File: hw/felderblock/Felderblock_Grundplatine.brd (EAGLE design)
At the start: 100 x 78 mm, 52 parts, among them IC2 LM2936, IC3 ULN2803, IC4 MCP2300X/P, J1 RJ11, J2 RJ11, M1 ARDUINO-NANO-3.0, T2 BC337, X1 TASTENSPERRE1, X2 TASTENSPERRE2, X3 SCHLUESSELSPERRE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

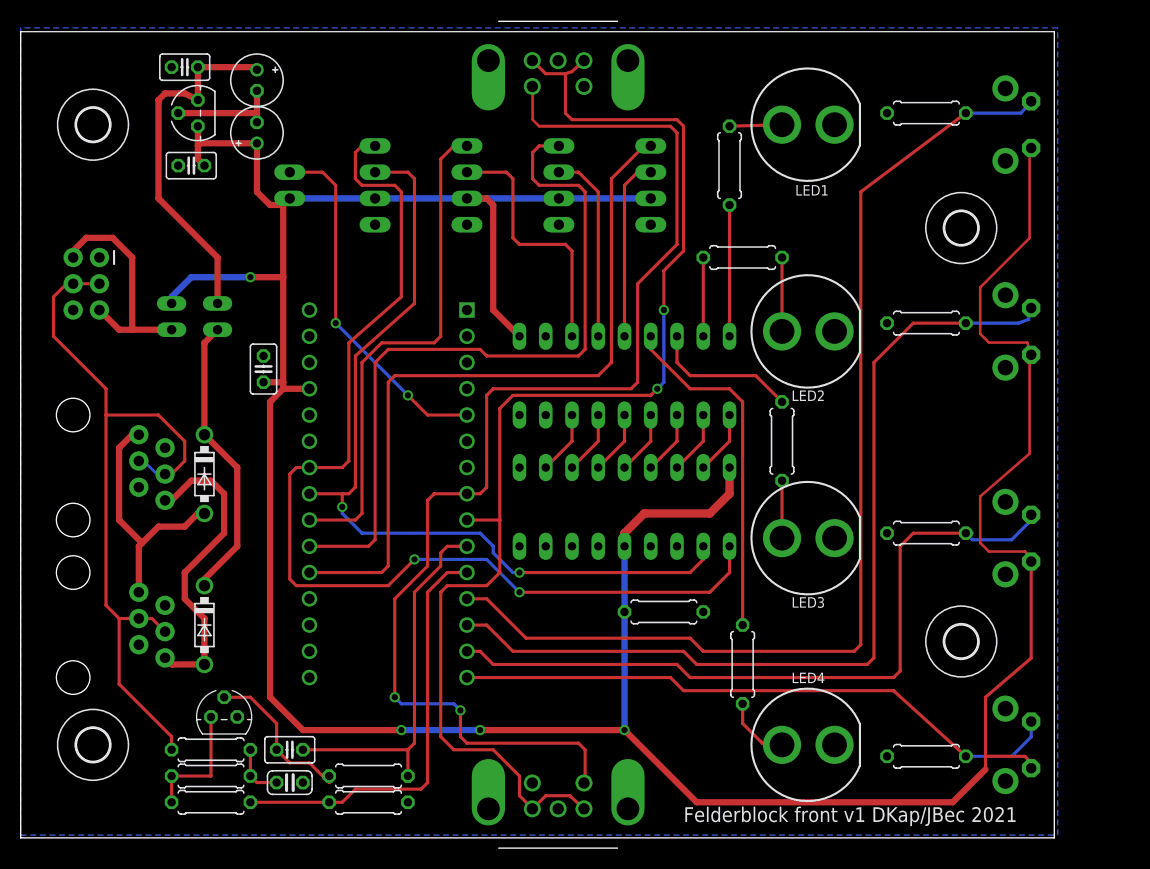
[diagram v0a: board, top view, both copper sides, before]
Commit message: CW and CCW split
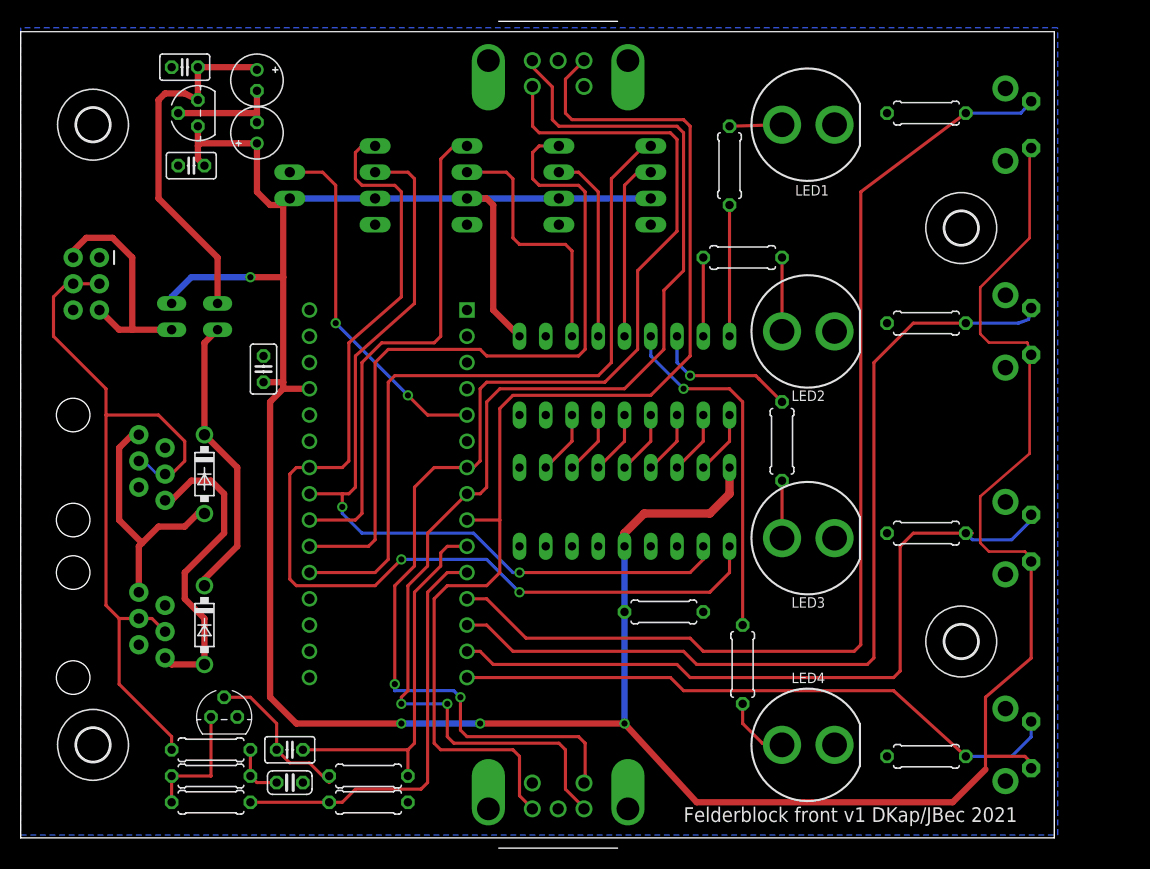
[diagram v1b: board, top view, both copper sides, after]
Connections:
- new net MI_REV: M1.J1.8, S5.A, S6.A
- net MI_FWD: no longer S5.A, S6.A
- net MI_SW: now also M1.J1.7; no longer M1.J1.8
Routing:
- net MI_REV: track 0.00 -> 120.1 mm, vias 0 -> 2
- net MI_FWD: track 123.0 -> 116.0 mm, vias 2 -> 0
- net MI_SW: track 121.4 -> 118.2 mm
- net FELD4_LEDD: track 33.9 -> 34.2 mm, vias 0 -> 1
- net FELD3_LEDD: vias 0 -> 1

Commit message: changed I2C connectors
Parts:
- removed X4: I2C, con-molex:22-23-2041
- added I2C: (no value), SparkFun-Connectors:JST-4-PTH-VERT
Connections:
- net +5V: now also I2C.3; no longer X4.2
- net GND: now also I2C.4; no longer X4.1
- net SCL: now also I2C.1; no longer X4.4
- net SDA: now also I2C.2; no longer X4.3
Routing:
- net SCL: track 102.9 -> 96.9 mm
- net SDA: track 82.2 -> 77.6 mm
- net +5V: vias 4 -> 5
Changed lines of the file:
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@@
 <?xml version="1.0" encoding="utf-8"?>
 <!DOCTYPE eagle SYSTEM "eagle.dtd">
-<eagle version="7.6.0">
+<eagle version="7.7.0">
 <drawing>
 <settings>
@@
 <attribute name="VALUE" x="67.945" y="45.085" size="1.27" layer="28" ratio="10" rot="MR0"/>
 </element>
-<element name="X4" library="con-molex" package="22-23-2041" value="I2C" x="34.29" y="64.135" smashed="yes" rot="MR90">
-<attribute name="MF" value="MOLEX" x="34.29" y="64.135" size="1.778" layer="28" rot="MR90" display="off"/>
-<attribute name="OC_NEWARK" value="38C0355" x="34.29" y="64.135" size="1.778" layer="28" rot="MR90" display="off"/>
-<attribute name="MPN" value="22-23-2041" x="34.29" y="64.135" size="1.778" layer="28" rot="MR90" display="off"/>
-<attribute name="OC_FARNELL" value="1462920" x="34.29" y="64.135" size="1.778" layer="28" rot="MR90" display="off"/>
-<attribute name="VALUE" x="38.1" y="59.055" size="1.016" layer="28" ratio="10" rot="MR90"/>
-</element>
 <element name="S5" library="alps" package="EC11B42" value="EC11B42AE" x="52" y="76.2" smashed="yes" rot="MR180">
 <attribute name="NAME" x="48.19" y="72.39" size="1.27" layer="26" rot="MR180"/>
@@
 <element name="C7" library="resistor" package="C025-025X050" value="1nF" x="26.035" y="9.525" smashed="yes" rot="R180">
 <attribute name="VALUE" x="28.321" y="12.319" size="1.27" layer="27" ratio="10" rot="R180"/>
+</element>
+<element name="I2C" library="SparkFun-Connectors" package="JST-4-PTH-VERT" value="" x="34.29" y="63.8175" rot="MR270">
+<attribute name="PROD_ID" value="CONN-13251" x="34.29" y="63.8175" size="1.778" layer="28" rot="MR270" display="off"/>
 </element>
 </elements>
@@
 <vertex x="0" y="79.375"/>
 </polygon>
-<contactref element="X4" pad="1"/>
 <contactref element="S5" pad="C"/>
 <contactref element="S6" pad="C"/>
@@
 <wire x1="22.86" y1="71.12" x2="22.86" y2="73.279" width="0.6096" layer="1"/>
 <wire x1="15.24" y1="71.12" x2="22.86" y2="71.12" width="0.6096" layer="1"/>
+<contactref element="I2C" pad="4"/>
 </signal>
 <signal name="LOCONET">
@@
 <contactref element="IC3" pad="10"/>
 <contactref element="X3" pad="1"/>
-<contactref element="X4" pad="2"/>
 <wire x1="97.6122" y1="38.1762" x2="97.6122" y2="47.8282" width="0.254" layer="1"/>
 <wire x1="92.837" y1="34.036" x2="97.6122" y2="38.1762" width="0.254" layer="1"/>
@@
 <wire x1="60.96" y1="62.865" x2="52.07" y2="62.865" width="0.6096" layer="16"/>
 <wire x1="52.07" y1="62.865" x2="43.18" y2="62.865" width="0.6096" layer="16"/>
-<wire x1="43.18" y1="62.865" x2="34.29" y2="62.865" width="0.6096" layer="16"/>
 <contactref element="IC4" pad="18"/>
-<wire x1="26.035" y1="62.865" x2="34.29" y2="62.865" width="0.6096" layer="16"/>
 <wire x1="27.94" y1="44.45" x2="25.4" y2="44.45" width="0.6096" layer="1"/>
 <wire x1="25.4" y1="44.45" x2="25.4" y2="45.085" width="0.6096" layer="1"/>
@@
 <wire x1="97.7646" y1="8.2804" x2="97.155" y2="8.89" width="0.3048" layer="1"/>
 <wire x1="97.155" y1="8.89" x2="93.345" y2="8.89" width="0.3048" layer="1"/>
+<contactref element="I2C" pad="3"/>
+<wire x1="26.035" y1="62.8175" x2="26.035" y2="62.865" width="0.6096" layer="16"/>
+<via x="26.035" y="62.8175" extent="1-16" drill="0.6" shape="square"/>
+<wire x1="43.18" y1="62.865" x2="43.1325" y2="62.8175" width="0.6096" layer="16"/>
+<wire x1="43.1325" y1="62.8175" x2="34.84" y2="62.8175" width="0.6096" layer="16"/>
+<wire x1="34.84" y1="62.8175" x2="34.7925" y2="62.865" width="0.6096" layer="16"/>
+<wire x1="34.7925" y1="62.865" x2="26.035" y2="62.865" width="0.6096" layer="16"/>
 </signal>
 <signal name="LN_TX">
@@
 <signal name="SDA">
 <contactref element="M1" pad="J2.8"/>
-<contactref element="X4" pad="3"/>
 <wire x1="27.94" y1="34.29" x2="31.115" y2="34.29" width="0.3048" layer="1"/>
-<wire x1="32.385" y1="34.925" x2="32.385" y2="47.625" width="0.3048" layer="1"/>
-<wire x1="32.385" y1="47.625" x2="38.1" y2="52.705" width="0.3048" layer="1"/>
-<wire x1="38.1" y1="52.705" x2="38.1" y2="64.77" width="0.3048" layer="1"/>
-<wire x1="38.1" y1="64.77" x2="37.465" y2="65.405" width="0.3048" layer="1"/>
-<wire x1="37.465" y1="65.405" x2="34.29" y2="65.405" width="0.3048" layer="1"/>
 <contactref element="IC4" pad="2"/>
 <wire x1="32.385" y1="34.925" x2="31.75" y2="34.29" width="0.3048" layer="1"/>
@@
 <wire x1="33.02" y1="30.48" x2="43.815" y2="30.48" width="0.3048" layer="16"/>
 <wire x1="43.815" y1="30.48" x2="47.625" y2="26.67" width="0.3048" layer="16"/>
+<contactref element="I2C" pad="2"/>
+<wire x1="32.385" y1="34.925" x2="32.385" y2="64.135" width="0.3048" layer="1"/>
+<wire x1="32.385" y1="64.135" x2="33.0675" y2="64.8175" width="0.3048" layer="1"/>
+<wire x1="33.0675" y1="64.8175" x2="34.84" y2="64.8175" width="0.3048" layer="1"/>
 </signal>
 <signal name="SCL">
 <contactref element="M1" pad="J2.7"/>
-<contactref element="X4" pad="4"/>
-<wire x1="36.83" y1="53.34" x2="31.75" y2="48.895" width="0.3048" layer="1"/>
-<wire x1="31.75" y1="48.895" x2="31.75" y2="37.465" width="0.3048" layer="1"/>
+<wire x1="31.75" y1="66.04" x2="31.75" y2="37.465" width="0.3048" layer="1"/>
 <wire x1="31.75" y1="37.465" x2="31.115" y2="36.83" width="0.3048" layer="1"/>
 <wire x1="31.115" y1="36.83" x2="27.94" y2="36.83" width="0.3048" layer="1"/>
-<wire x1="36.83" y1="53.34" x2="36.83" y2="63.5" width="0.3048" layer="1"/>
-<wire x1="36.83" y1="63.5" x2="36.195" y2="64.135" width="0.3048" layer="1"/>
-<wire x1="36.195" y1="64.135" x2="33.02" y2="64.135" width="0.3048" layer="1"/>
-<wire x1="33.02" y1="64.135" x2="32.385" y2="64.77" width="0.3048" layer="1"/>
-<wire x1="32.385" y1="64.77" x2="32.385" y2="67.31" width="0.3048" layer="1"/>
-<wire x1="32.385" y1="67.31" x2="33.02" y2="67.945" width="0.3048" layer="1"/>
-<wire x1="33.02" y1="67.945" x2="34.29" y2="67.945" width="0.3048" layer="1"/>
 <contactref element="IC4" pad="1"/>
 <via x="36.83" y="27.94" extent="1-16" drill="0.6" shape="square"/>
@@
 <wire x1="66.675" y1="24.765" x2="68.58" y2="26.67" width="0.3048" layer="1"/>
 <wire x1="68.58" y1="26.67" x2="68.58" y2="29.21" width="0.3048" layer="1"/>
+<contactref element="I2C" pad="1"/>
+<wire x1="31.75" y1="66.04" x2="32.5275" y2="66.8175" width="0.3048" layer="1"/>
+<wire x1="32.5275" y1="66.8175" x2="34.84" y2="66.8175" width="0.3048" layer="1"/>
 </signal>
 <signal name="FELD3_LED">
